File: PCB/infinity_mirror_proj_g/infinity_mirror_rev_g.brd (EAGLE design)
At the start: 51 x 37 mm, 31 parts, among them J1 POWER_JACKPTH_BREAD, J2 LED_CAP, J3 SERIAL, Q3 BSS138, U1 3.3LDO

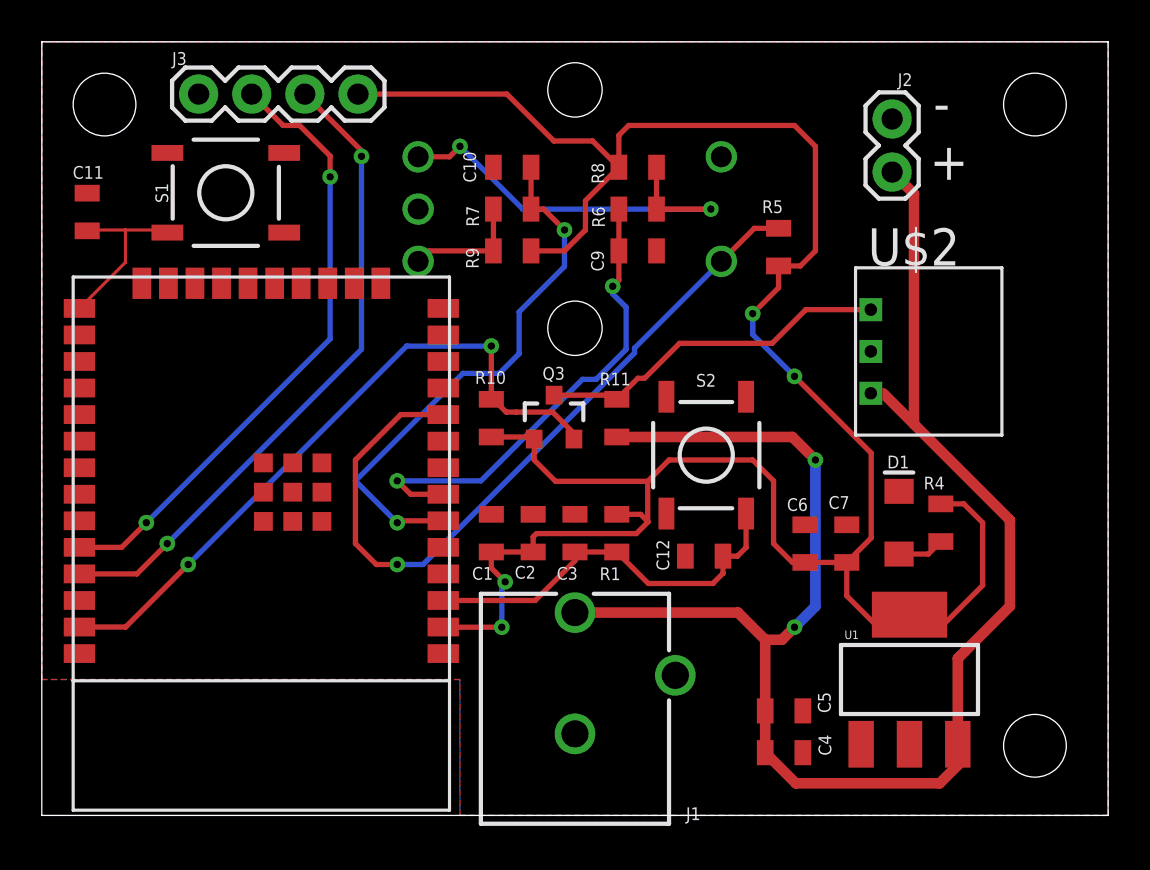
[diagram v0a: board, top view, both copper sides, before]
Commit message: serial connector from 4pin to 3pin. changed led data gpio to reduce trace length
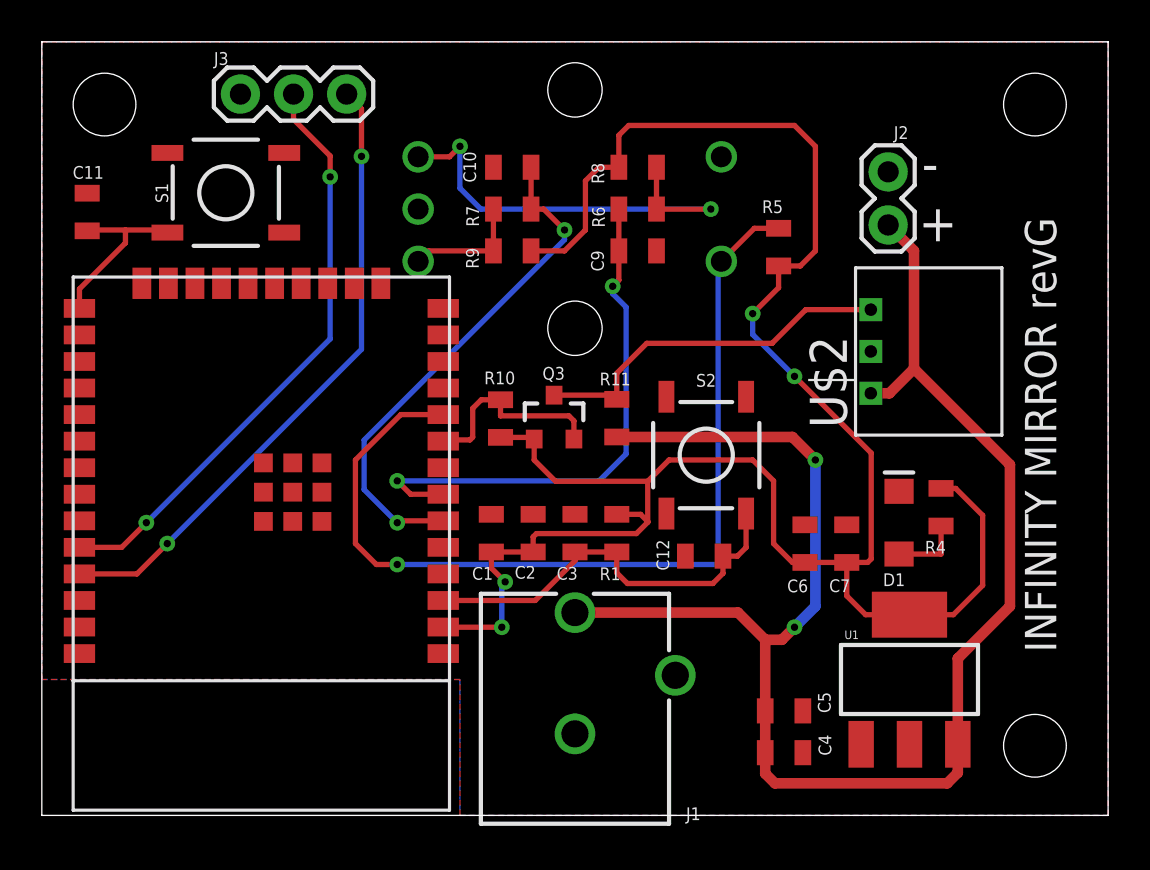
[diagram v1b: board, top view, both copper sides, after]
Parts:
- J3: device SparkFun-Connectors:1X04 -> SparkFun-Connectors:1X03
- moved J2 2.54 mm to (40.5, 28.2)
- moved J3 2.00 mm to (9.50, 34.5)
- moved R4 0.74 mm to (43.0, 14.7)
- moved R10 0.44 mm to (21.9, 19.0)
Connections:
- removed net IO23: Q3.2, R10.1, U$1.P$37
- new net IO33: Q3.2, R10.1, U$1.P$9
- net VCC_2: no longer J3.4
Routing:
- net IO23: track 32.8 -> 0.00 mm, vias 2 -> 0
- net VCC_2: track 113.3 -> 100.0 mm
- net IO33: track 0.00 -> 9.72 mm
- net BUTTON: track 36.5 -> 44.8 mm
- net ENC_B: track 23.1 -> 26.0 mm
- net VCC_1: track 79.6 -> 77.9 mm
- net ENC_A: track 26.2 -> 24.9 mm
- net U0RXD: track 29.8 -> 28.6 mm
- net N$2: track 20.0 -> 21.2 mm
- net LED+: track 2.25 -> 3.35 mm
- net U0TXD: track 31.3 -> 30.4 mm
- net LED_DATA: track 17.0 -> 17.7 mm
- net EN: track 19.1 -> 19.7 mm
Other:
- board text added: "INFINITY MIRROR revG"

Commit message: rev g purchased
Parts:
- moved U$2 3.33 mm to (42.2, 24.4), turned to 0 degrees
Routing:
- net LED_DATA: track 17.7 -> 23.4 mm
- net VCC_1: track 77.9 -> 81.1 mm
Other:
- board text added: "BOOT"
- board text added: "EN"
- board text added: "INFINITY MIRROR V1.0"
- board text added: "RX"
- board text added: "TX"
- board text removed: "INFINITY MIRROR revG"
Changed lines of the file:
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@@
 <text x="41.94" y="27.46" size="1.778" layer="21">+</text>
 <text x="42.09" y="30.3" size="1.778" layer="21">-</text>
-<text x="48.52" y="7.8" size="1.5" layer="112" rot="R90">INFINITY MIRROR revG</text>
+<text x="49.66" y="7.69" size="1.5" layer="21" rot="R90">INFINITY MIRROR V1.0</text>
+<text x="35.54" y="16.35" size="1" layer="112" rot="R90">EN</text>
+<text x="13.57" y="27.91" size="1" layer="112" rot="R90">BOOT</text>
+<text x="12.55" y="36.54" size="0.6096" layer="21" rot="R180">RX</text>
+<text x="14.01" y="36.01" size="0.6096" layer="21">TX</text>
 </plain>
 <attributes>
@@
 </element>
 <element name="J1" library="SparkFun-Connectors" library_urn="urn:adsk.eagle:library:513" package="POWER_JACK_PTH_BREAD" package3d_urn="urn:adsk.eagle:package:38228/1" value="POWER_JACKPTH_BREAD" x="25.5" y="-4" smashed="yes">
-<attribute name="NAME" x="30.8102" y="-0.226" size="0.6096" layer="25" font="vector" ratio="20"/>
+<attribute name="NAME" x="30.8102" y="1.774" size="0.6096" layer="25" font="vector" ratio="20"/>
 <attribute name="PROD_ID" value="PRT-10811" x="25.5" y="-4" size="1.778" layer="27" display="off"/>
 </element>
@@
 <attribute name="VALUE" x="43.11" y="16.409" size="0.6096" layer="27" font="vector" ratio="20" rot="R180" align="top-center"/>
 </element>
-<element name="U$2" library="infinity_mirror_revd" package="3-PIN-JST" value="3-PIN-JST" x="39.65" y="22.19" smashed="yes" rot="R90">
-<attribute name="NAME" x="36.73" y="22.93" size="1.778" layer="21" rot="R270"/>
+<element name="U$2" library="infinity_mirror_revd" package="3-PIN-JST" value="3-PIN-JST" x="42.19" y="24.35" smashed="yes">
+<attribute name="NAME" x="41.29" y="25.86" size="0.6096" layer="21" rot="R180"/>
 </element>
 <element name="U$3" library="infinity_mirror_revd" package="PEC11R-4320F-S0012" value="PEC11R" x="25.5" y="29" smashed="yes" rot="MR90">
-<attribute name="NAME" x="34.5" y="30" size="1.778" layer="22" rot="MR90"/>
-<attribute name="VALUE" x="23.66" y="23.14" size="1.778" layer="22" rot="MR180"/>
+<attribute name="NAME" x="33.37" y="34.29" size="0.6096" layer="22" rot="MR0"/>
+<attribute name="VALUE" x="34.86" y="24.66" size="1.778" layer="22" rot="MR90"/>
 </element>
 <element name="R5" library="_111_IH" package="0805" value="10k" x="35.24" y="27.18" smashed="yes" rot="R270">
@@
 </element>
 <element name="S1" library="SparkFun-Switches" package="TACTILE_SWITCH_SMD_5.2MM" value="SWITCH" x="8.8" y="29.78" smashed="yes">
-<attribute name="NAME" x="6.043" y="29.77" size="0.6096" layer="25" font="vector" ratio="20" rot="R90" align="bottom-center"/>
+<attribute name="NAME" x="5.953" y="29" size="0.6096" layer="25" font="vector" ratio="20" rot="R90" align="bottom-center"/>
 <attribute name="PROD_ID" value="SWCH-14139" x="8.8" y="29.78" size="1.778" layer="27" display="off"/>
 </element>
 <element name="S2" library="SparkFun-Switches" package="TACTILE_SWITCH_SMD_5.2MM" value="SWITCH" x="31.78" y="17.23" smashed="yes" rot="R90">
-<attribute name="NAME" x="31.77" y="21.113" size="0.6096" layer="25" font="vector" ratio="20" rot="R180" align="bottom-center"/>
+<attribute name="NAME" x="31.26" y="20.603" size="0.6096" layer="25" font="vector" ratio="20" rot="R180" align="bottom-center"/>
 <attribute name="PROD_ID" value="SWCH-14139" x="31.78" y="17.23" size="1.778" layer="27" rot="R90" display="off"/>
 </element>
@@
 <element name="J3" library="SparkFun-Connectors" library_urn="urn:adsk.eagle:library:513" package="1X03" package3d_urn="urn:adsk.eagle:package:38063/1" value="SERIAL" x="9.5" y="34.5" smashed="yes">
 <attribute name="NAME" x="8.23" y="35.897" size="0.6096" layer="25" font="vector" ratio="20"/>
-<attribute name="VALUE" x="11.15" y="35.988" size="0.6096" layer="27" font="vector" ratio="20"/>
+<attribute name="VALUE" x="7.782" y="33.08" size="0.6096" layer="27" font="vector" ratio="20" rot="R90"/>
 </element>
 <element name="J2" library="SparkFun-Connectors" package="1X02" value="LED_CAP" x="40.48" y="28.24" smashed="yes" rot="R90">
@@
 </elements>
 <signals>
-<signal name="GND" airwireshidden="yes">
+<signal name="GND">
 <contactref element="C3" pad="2"/>
 <contactref element="C1" pad="2"/>
@@
 <contactref element="U$1" pad="P$38"/>
 <contactref element="J3" pad="1"/>
-<wire x1="32.5" y1="31.5" x2="40.48" y2="30.78" width="0" layer="19" extent="1-1"/>
-<wire x1="29.4" y1="27" x2="32.5" y2="31.5" width="0" layer="19" extent="1-1"/>
-<wire x1="21.6" y1="31" x2="29.4" y2="27" width="0" layer="19" extent="1-1"/>
-<wire x1="18" y1="29" x2="21.6" y2="31" width="0" layer="19" extent="1-1"/>
-<wire x1="39.65" y1="22.19" x2="40.48" y2="30.78" width="0" layer="19" extent="1-1"/>
-<wire x1="41" y1="15.5" x2="39.65" y2="22.19" width="0" layer="19" extent="1-1"/>
-<wire x1="38.5" y1="13.9" x2="41" y2="15.5" width="0" layer="19" extent="1-1"/>
-<wire x1="36.5" y1="13.9" x2="38.5" y2="13.9" width="0" layer="19" extent="1-1"/>
-<wire x1="30.78" y1="12.4" x2="36.5" y2="13.9" width="0" layer="19" extent="1-1"/>
-<wire x1="29.875" y1="14.436" x2="30.78" y2="12.4" width="0" layer="19" extent="1-1"/>
-<wire x1="25.5" y1="14.4" x2="29.875" y2="14.436" width="0" layer="19" extent="1-1"/>
-<wire x1="23.5" y1="14.4" x2="25.5" y2="14.4" width="0" layer="19" extent="1-1"/>
-<wire x1="21.5" y1="14.4" x2="23.5" y2="14.4" width="0" layer="19" extent="1-1"/>
-<wire x1="30.3" y1="6.7" x2="30.78" y2="12.4" width="0" layer="19" extent="1-1"/>
-<wire x1="25.5" y1="3.9" x2="30.3" y2="6.7" width="0" layer="19" extent="1-1"/>
-<wire x1="36.4" y1="5" x2="30.3" y2="6.7" width="0" layer="19" extent="1-1"/>
-<wire x1="36.4" y1="3" x2="36.4" y2="5" width="0" layer="19" extent="1-1"/>
-<wire x1="39.1886" y1="3.4012" x2="36.4" y2="3" width="0" layer="19" extent="1-1"/>
-<wire x1="19.2" y1="7.74" x2="21.5" y2="14.4" width="0" layer="19" extent="1-1"/>
-<wire x1="9.5" y1="34.5" x2="18" y2="29" width="0" layer="19" extent="1-1"/>
-<wire x1="6.006" y1="31.685" x2="9.5" y2="34.5" width="0" layer="19" extent="1-1"/>
-<wire x1="2.17" y1="29.76" x2="6.006" y2="31.685" width="0" layer="19" extent="1-1"/>
-<wire x1="1.8" y1="7.74" x2="19.2" y2="7.74" width="0" layer="19" extent="1-1"/>
 </signal>
 <signal name="U0TXD">
@@
 <wire x1="36" y1="9" x2="35.4" y2="8.4" width="0.508" layer="1"/>
 <wire x1="35.4" y1="8.4" x2="34.6" y2="8.4" width="0.508" layer="1"/>
-<wire x1="46.3048" y1="16.77625625" x2="41.715528125" y2="21.365528125" width="0.508" layer="1"/>
-<wire x1="46.3048" y1="16.77625625" x2="46.3048" y2="10" width="0.508" layer="1"/>
 <wire x1="43.8114" y1="7.5066" x2="46.3048" y2="10" width="0.508" layer="1"/>
-<wire x1="41.715528125" y1="21.365528125" x2="41.715528125" y2="27.004471875" width="0.508" layer="1"/>
-<wire x1="41.715528125" y1="27.004471875" x2="40.48" y2="28.24" width="0.508" layer="1"/>
+<wire x1="46.3048" y1="10" x2="46.3048" y2="25.4152" width="0.508" layer="1"/>
+<wire x1="46.3048" y1="25.4152" x2="43.48" y2="28.24" width="0.508" layer="1"/>
+<wire x1="43.48" y1="28.24" x2="40.48" y2="28.24" width="0.508" layer="1"/>
 <wire x1="43.8114" y1="2.0412" x2="43.8114" y2="3.4012" width="0.508" layer="1"/>
 <wire x1="43.8114" y1="2.0412" x2="43.3052" y2="1.535" width="0.508" layer="1"/>
 <wire x1="43.8114" y1="3.4012" x2="43.8114" y2="7.5066" width="0.508" layer="1"/>
-<wire x1="39.65" y1="20.19" x2="40.54" y2="20.19" width="0.508" layer="1"/>
-<wire x1="40.54" y1="20.19" x2="41.715528125" y2="21.365528125" width="0.508" layer="1"/>
+<wire x1="40.48" y1="28.24" x2="40.48" y2="24.64" width="0.508" layer="1"/>
+<wire x1="40.48" y1="24.64" x2="40.19" y2="24.35" width="0.508" layer="1"/>
 </signal>
 <signal name="LED+">
@@
 <wire x1="27.5" y1="19.9" x2="27.5" y2="21.1469125" width="0.254" layer="1"/>
 <wire x1="28.9330875" y1="22.58" x2="27.5" y2="21.1469125" width="0.254" layer="1"/>
-<wire x1="36.54" y1="24.19" x2="34.93" y2="22.58" width="0.254" layer="1"/>
-<wire x1="36.54" y1="24.19" x2="39.65" y2="24.19" width="0.254" layer="1"/>
-<wire x1="34.93" y1="22.58" x2="28.9330875" y2="22.58" width="0.254" layer="1"/>
+<wire x1="44.19" y1="22.58" x2="44.19" y2="24.35" width="0.254" layer="1"/>
+<wire x1="44.19" y1="22.58" x2="28.9330875" y2="22.58" width="0.254" layer="1"/>
 </signal>
 <signal name="N$2">
@@
 <mfgpreviewcolor name="substratecolor" color="0xFF786E46"/>
 </mfgpreviewcolors>
+<errors>
+</errors>
 </board>
 </drawing>
